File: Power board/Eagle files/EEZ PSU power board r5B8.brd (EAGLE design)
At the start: 150 x 74 mm, 270 parts, among them IC1 LTC3864, IC10 REF5025, IC11 DAC8552, IC12 ADG465SOT-23, IC13 TS5A9411DCKT, IC14 ADS1120, IC15 LP339D, IC2 MC79L05, IC3 MC78L05, IC4 LM5574, IC5 LP2951SO8, IC6 TL072D, IC7 TL072D, IC8 OP27GSZ, IC9 MCP23S08-E/SO, Q1 SUD19P06-60, Q10 MMBT5401, Q11 MMBT5401, Q12 MMBT5551, Q13 MMBT5551, Q14 BSS84P, Q15 2N7002, Q16 MMBT5551, Q17 MMBT5401, Q18 MMBT5551, Q19 MMBT5551, Q2 MMBT5401, Q3 2N7002, Q4 IRFP250N, Q5 BC857C, Q6 BC846C, Q7 BCP56-16.115, Q8 IRFR5410, Q9 BCP56-16.115, X1 282836-3, X2 282836-2, X3 SSW-113-02-T-D-RA

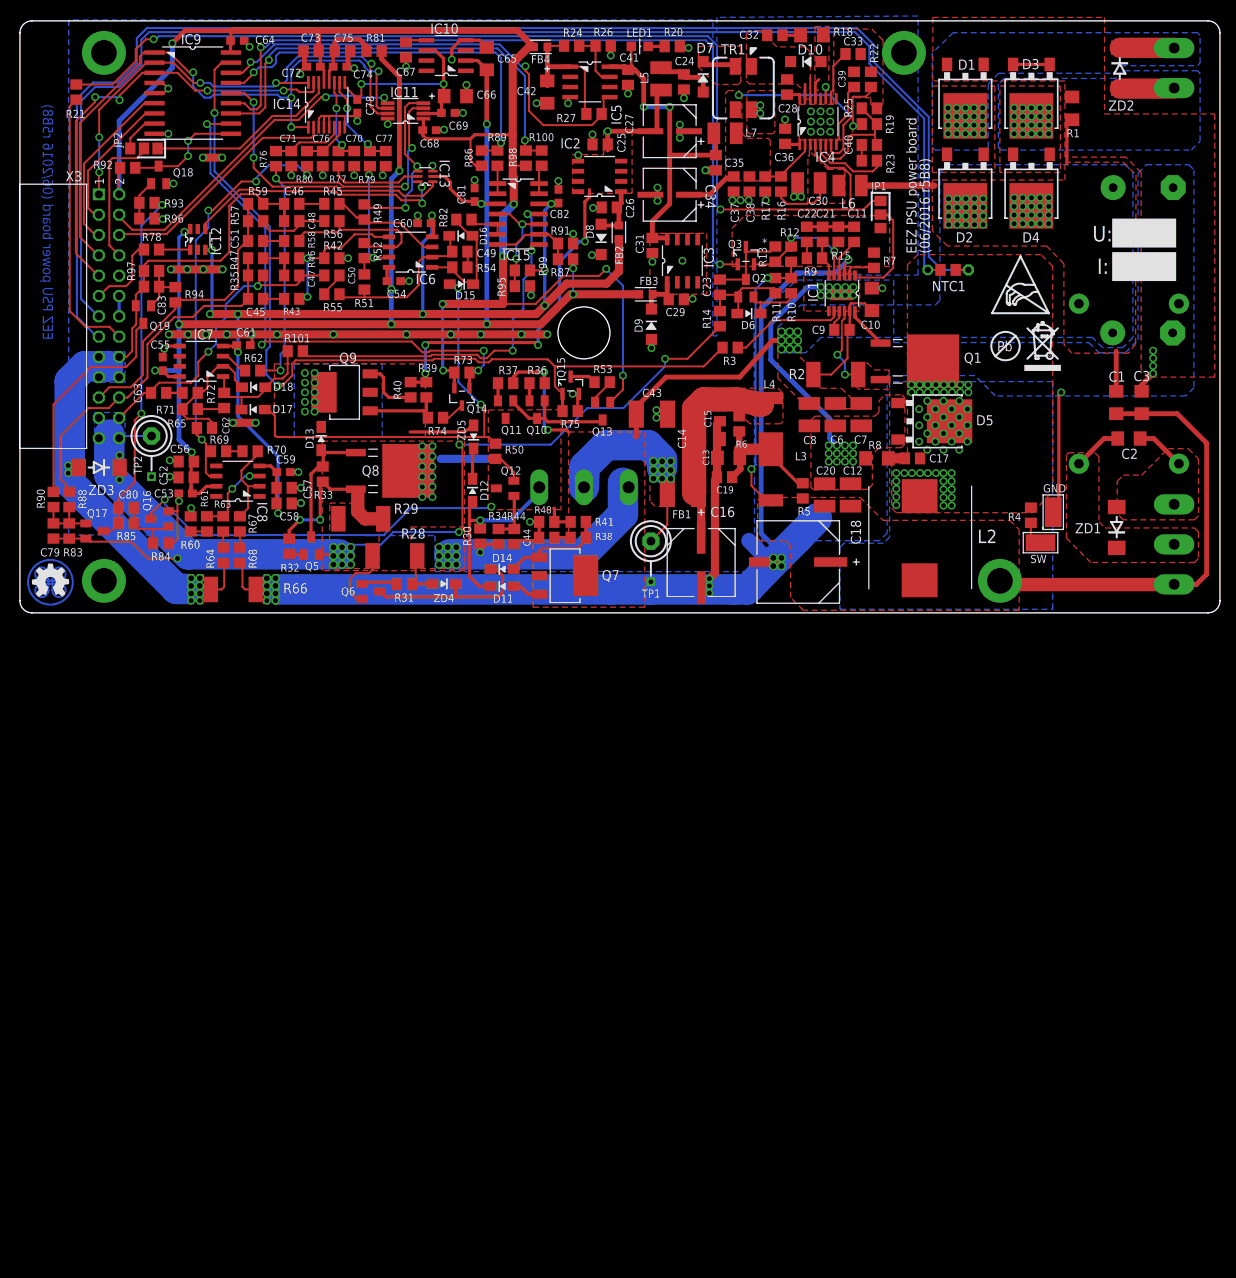
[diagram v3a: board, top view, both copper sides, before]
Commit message: PCB fiducials, outlines, milling bridges
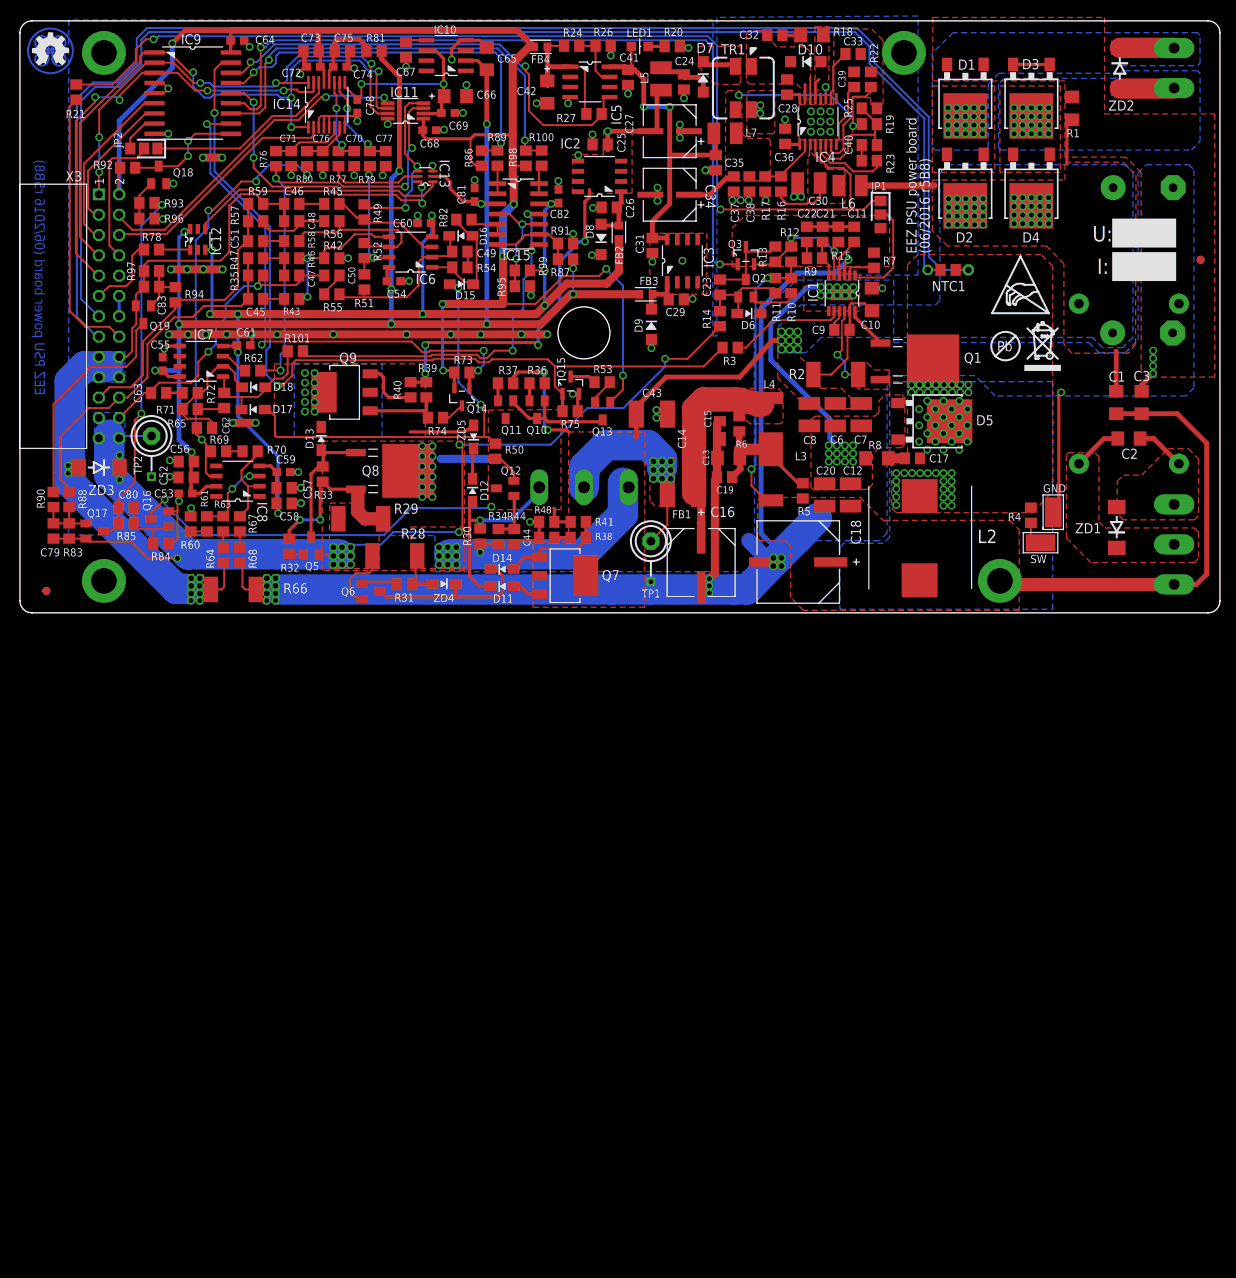
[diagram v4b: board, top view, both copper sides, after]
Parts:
- added U$11, U$12: FIDUCIAL_2, EEZ_Lib1:FIDUCIAL_DUAL
- moved EEZ_SIGNATURE 66.4 mm to (3.81, 146.3)
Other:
- board text removed: "*"
- board text removed: "* Check instructions for R13 installation"
